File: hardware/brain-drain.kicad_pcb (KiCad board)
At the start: 4 copper layers, 180 x 110 mm, 311 parts, among them J10 SATA 22-pin, J11 SATA 22-pin, J12 SATA 22-pin, J13 SATA 22-pin, J21 KPJX-4S-S, J3 microSD, J4 RJ45 GbE magjack UDE RB1-125B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, J40 Fan GND/5V/TACH/PWM, J41 OLED GND/VCC/SCL/SDA, J5 USB-C rpiboot, J50 M.2 M-key, J6 nRPIBOOT, J7 UART0 GND/TX/RX, M1 CM5002016, Q1 2N7002, Q20 AO4407A, Q31 P-FET -30V 6A DFN3x3, Q32 P-FET -30V 6A DFN3x3, Q33 P-FET -30V 6A DFN3x3, Q34 P-FET -30V 6A DFN3x3, Q41 P-FET -30V 6A DFN3x3, Q42 P-FET -30V 6A DFN3x3, Q43 P-FET -30V 6A DFN3x3, Q44 P-FET -30V 6A DFN3x3, Q51 2N7002, Q52 2N7002, Q53 2N7002, Q54 2N7002, Q61 2N7002, Q62 2N7002, Q63 2N7002, Q64 2N7002, SW1 DIP x8, SW3 door microswitch, U1 USB5744/2G, U10 ASM1153E, U11 ASM1153E, U12 ASM1153E, U13 ASM1153E, U2 USB5744/2G, U20 TPS56637RPAR, U21 TPS56637RPAR, U22 AP63203WU-7, U3 AP2112K-1.2, U50 TPS22965DSGR, U51 AP63203WU-7, U52 TPS22965DSGR, Y1 25MHz CL=20pF, Y10 30MHz CL=16pF, Y11 30MHz CL=16pF, Y12 30MHz CL=16pF, Y13 30MHz CL=16pF, Y2 25MHz CL=20pF

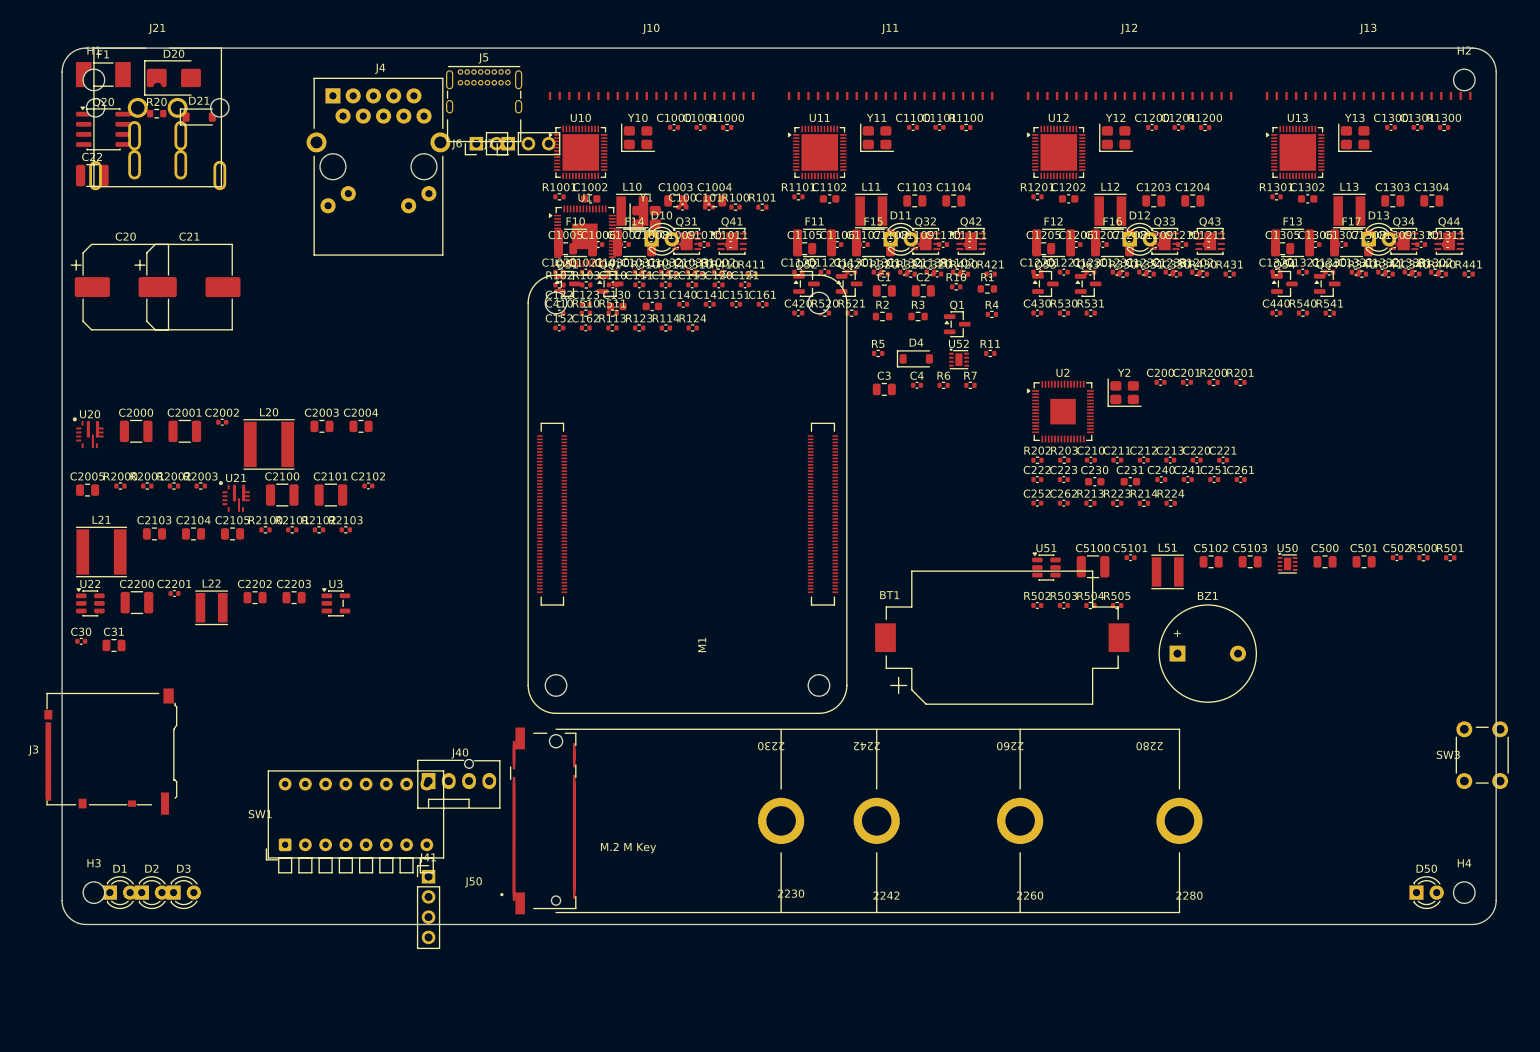
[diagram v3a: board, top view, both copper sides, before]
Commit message: docs: README with logo and renders, docs index, STATUS, USAGE, HISTORY, testing tracker, AGENT.md, changelog; enclosure refinements and renders; routing pipeline
Co-Authored-By: Claude Fable 5.1 <noreply@anthropic.com>
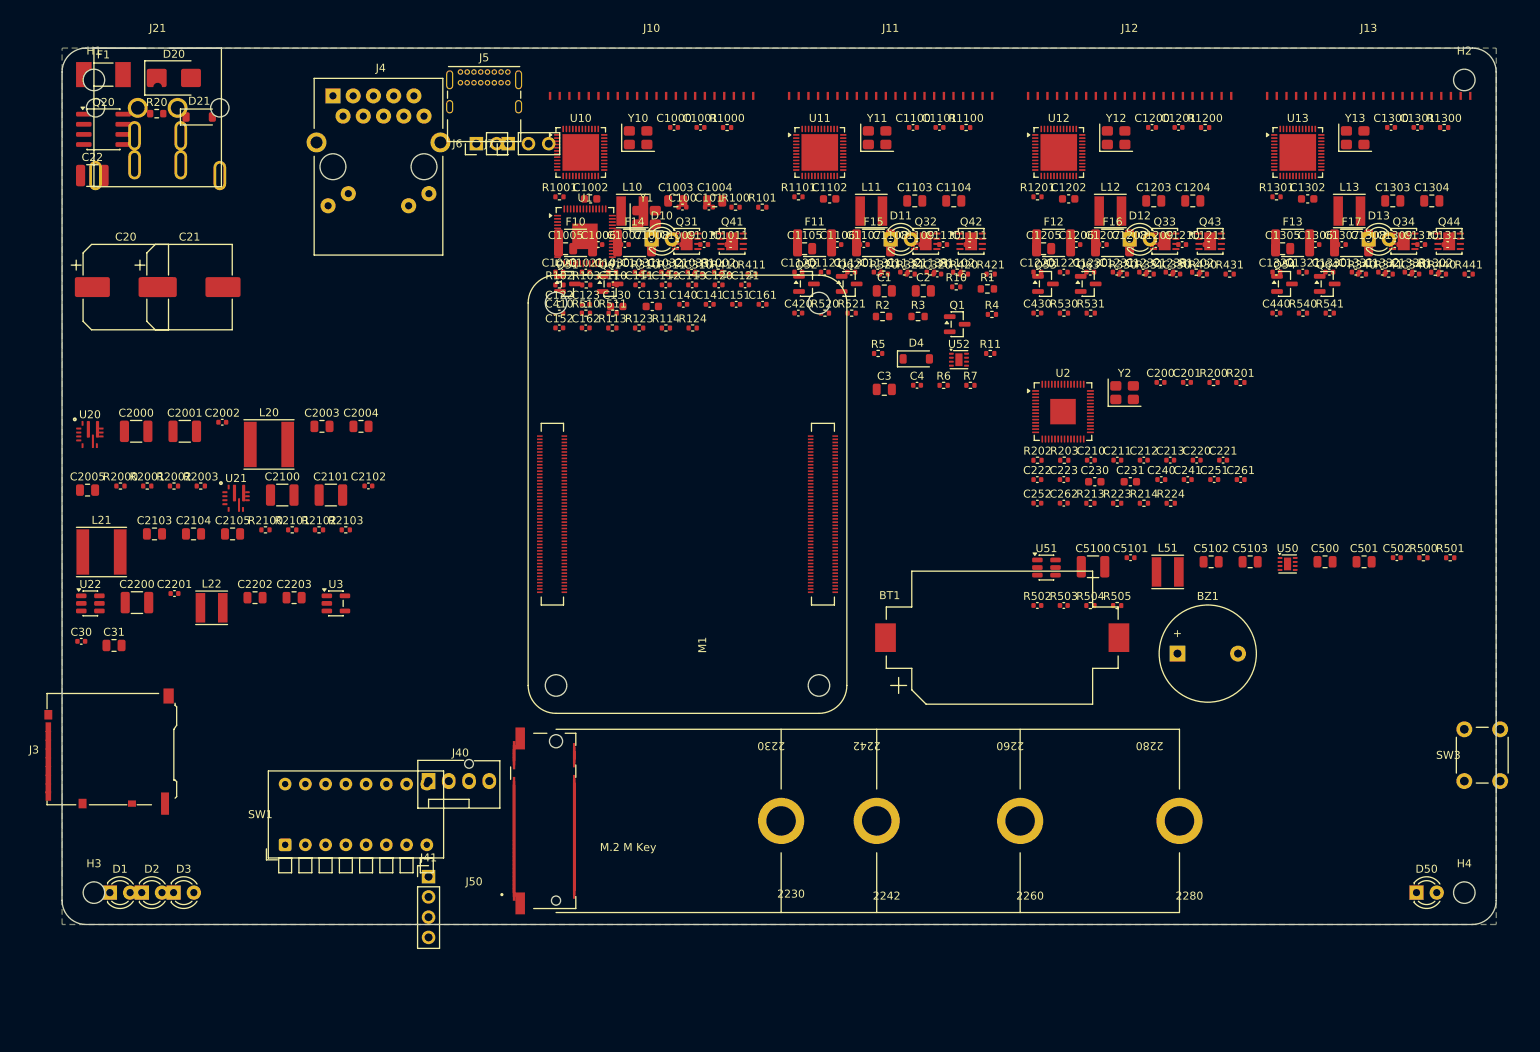
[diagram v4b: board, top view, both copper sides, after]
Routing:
- added copper zone on In2.Cu, net +12V
- added copper zone on In2.Cu, net +3V3
- added copper zone on In2.Cu, net 5V_HDD
- added copper zone on In2.Cu, net 5V_SYS
- added copper zone on B.Cu, net GND
- added copper zone on In1.Cu, net GND

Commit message: hw(board): DRC-clean placement (pad rotation fix, packer with capacity checks, USB-C on the left wall, DIN pad fix)
Co-Authored-By: Claude Fable 5.1 <noreply@anthropic.com>
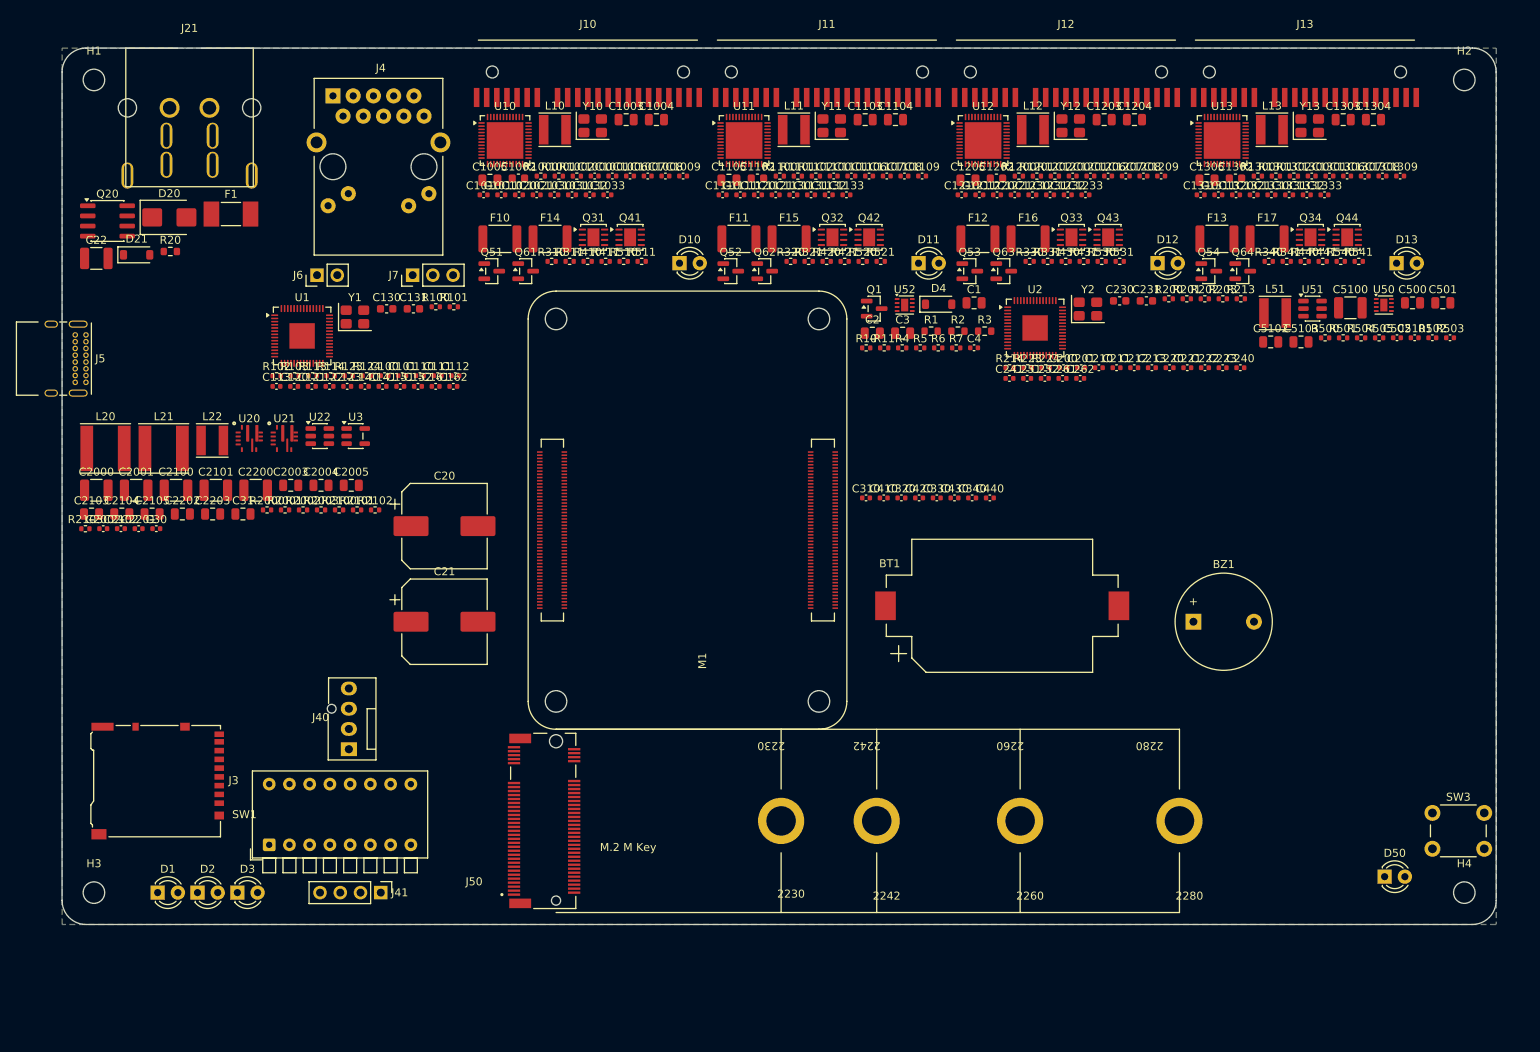
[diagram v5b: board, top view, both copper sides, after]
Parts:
- BT1: renamed from R20; value 100k -> CR2032; footprint Resistor_SMD:R_0603_1608Metric -> Battery:BatteryHolder_Keystone_1060_1x2032
- BZ1: renamed from C2002; value 100n 25V -> 5V magnetic; footprint Capacitor_SMD:C_0402_1005Metric -> Buzzer_Beeper:Buzzer_12x9.5RM7.6
- C1: renamed from C110; value 100n -> 22u 10V; footprint Capacitor_SMD:C_0402_1005Metric -> Capacitor_SMD:C_0805_2012Metric
- C100: renamed from R201; value 10k -> 33p; footprint Resistor_SMD:R_0402_1005Metric -> Capacitor_SMD:C_0402_1005Metric
- C1002: renamed from F14; value 2A hold 1812 -> 2.2u; footprint Fuse:Fuse_1812_4532Metric -> Capacitor_SMD:C_0603_1608Metric
- C1003: renamed from D10; value blue bay activity -> 10u 10V; footprint LED_THT:LED_D3.0mm -> Capacitor_SMD:C_0805_2012Metric
- C1004: renamed from R1002; value 470 -> 10u 10V; footprint Resistor_SMD:R_0402_1005Metric -> Capacitor_SMD:C_0805_2012Metric
- C1005: renamed from F10; value 3A hold 1812 -> 10u 10V; footprint Fuse:Fuse_1812_4532Metric -> Capacitor_SMD:C_0805_2012Metric
- C1006: renamed from R1100; value 12.1k 1% -> 100n; footprint Resistor_SMD:R_0402_1005Metric -> Capacitor_SMD:C_0402_1005Metric
- C1007: renamed from R1101; value 10k -> 100n; footprint Resistor_SMD:R_0402_1005Metric -> Capacitor_SMD:C_0402_1005Metric
- C1008: renamed from C1102; value 2.2u -> 100n; footprint Capacitor_SMD:C_0603_1608Metric -> Capacitor_SMD:C_0402_1005Metric
- C1009: renamed from L11; value 4.7u 1A -> 100n; footprint Inductor_SMD:L_Taiyo-Yuden_NR-40xx -> Capacitor_SMD:C_0402_1005Metric
- C101: renamed from R202; value 10k -> 33p; footprint Resistor_SMD:R_0402_1005Metric -> Capacitor_SMD:C_0402_1005Metric
- C1010: renamed from C1103; value 10u 10V -> 100n; footprint Capacitor_SMD:C_0805_2012Metric -> Capacitor_SMD:C_0402_1005Metric
- C1011: renamed from C1104; value 10u 10V -> 100n; footprint Capacitor_SMD:C_0805_2012Metric -> Capacitor_SMD:C_0402_1005Metric
- C1020: renamed from C1105; value 10u 10V -> 100n; footprint Capacitor_SMD:C_0805_2012Metric -> Capacitor_SMD:C_0402_1005Metric
- C1030: renamed from C1107; value 100n -> 10n
- C1031: renamed from C1108; value 100n -> 10n
- C1032: renamed from C1109; value 100n -> 10n
- C1033: renamed from C1110; value 100n -> 10n
- C110: renamed from R203; value 200k -> 100n; footprint Resistor_SMD:R_0402_1005Metric -> Capacitor_SMD:C_0402_1005Metric
- C1100: renamed from C1207; value 100n -> 22p
- C1101: renamed from C1208; value 100n -> 22p
- C1102: renamed from C1203; value 10u 10V -> 2.2u; footprint Capacitor_SMD:C_0805_2012Metric -> Capacitor_SMD:C_0603_1608Metric
- C1103: renamed from R1201; value 10k -> 10u 10V; footprint Resistor_SMD:R_0402_1005Metric -> Capacitor_SMD:C_0805_2012Metric
- C1104: renamed from C1202; value 2.2u -> 10u 10V; footprint Capacitor_SMD:C_0603_1608Metric -> Capacitor_SMD:C_0805_2012Metric
- C1105: renamed from L12; value 4.7u 1A -> 10u 10V; footprint Inductor_SMD:L_Taiyo-Yuden_NR-40xx -> Capacitor_SMD:C_0805_2012Metric
- C1111: renamed from C1230; value 10n -> 100n
- C1120: renamed from C1231; value 10n -> 100n
- C1121: renamed from C1232; value 10n -> 100n
- C1131: renamed from D12; value blue bay activity -> 10n; footprint LED_THT:LED_D3.0mm -> Capacitor_SMD:C_0402_1005Metric
- C1132: renamed from R1202; value 470 -> 10n; footprint Resistor_SMD:R_0402_1005Metric -> Capacitor_SMD:C_0402_1005Metric
- C1133: renamed from F12; value 3A hold 1812 -> 10n; footprint Fuse:Fuse_1812_4532Metric -> Capacitor_SMD:C_0402_1005Metric
- C1200: renamed from C1333; value 10n -> 22p
- C1201: renamed from D13; value blue bay activity -> 22p; footprint LED_THT:LED_D3.0mm -> Capacitor_SMD:C_0402_1005Metric
- C1202: renamed from C1321; value 100n -> 2.2u; footprint Capacitor_SMD:C_0402_1005Metric -> Capacitor_SMD:C_0603_1608Metric
- C1203: renamed from C1310; value 100n -> 10u 10V; footprint Capacitor_SMD:C_0402_1005Metric -> Capacitor_SMD:C_0805_2012Metric
- C1204: renamed from C1311; value 100n -> 10u 10V; footprint Capacitor_SMD:C_0402_1005Metric -> Capacitor_SMD:C_0805_2012Metric
- C1205: renamed from C1320; value 100n -> 10u 10V; footprint Capacitor_SMD:C_0402_1005Metric -> Capacitor_SMD:C_0805_2012Metric
- C1206: renamed from R1302; value 470 -> 100n; footprint Resistor_SMD:R_0402_1005Metric -> Capacitor_SMD:C_0402_1005Metric
- C1207: renamed from F13; value 3A hold 1812 -> 100n; footprint Fuse:Fuse_1812_4532Metric -> Capacitor_SMD:C_0402_1005Metric
- C1208: renamed from F17; value 2A hold 1812 -> 100n; footprint Fuse:Fuse_1812_4532Metric -> Capacitor_SMD:C_0402_1005Metric
- C1209: renamed from Q31; value P-FET -30V 6A DFN3x3 -> 100n; footprint Package_DFN_QFN:DFN-8-1EP_3x3mm_P0.65mm_EP1.5x2.25mm -> Capacitor_SMD:C_0402_1005Metric
- C1210: renamed from Q41; value P-FET -30V 6A DFN3x3 -> 100n; footprint Package_DFN_QFN:DFN-8-1EP_3x3mm_P0.65mm_EP1.5x2.25mm -> Capacitor_SMD:C_0402_1005Metric
- C1211: renamed from Q51; value 2N7002 -> 100n; footprint Package_TO_SOT_SMD:SOT-23 -> Capacitor_SMD:C_0402_1005Metric
- C1220: renamed from Q61; value 2N7002 -> 100n; footprint Package_TO_SOT_SMD:SOT-23 -> Capacitor_SMD:C_0402_1005Metric
- C1221: renamed from R310; value 100k -> 100n; footprint Resistor_SMD:R_0402_1005Metric -> Capacitor_SMD:C_0402_1005Metric
- C1230: renamed from R311; value 10k -> 10n; footprint Resistor_SMD:R_0402_1005Metric -> Capacitor_SMD:C_0402_1005Metric
- C1231: renamed from C310; value 100n -> 10n
- C1232: renamed from R410; value 100k -> 10n; footprint Resistor_SMD:R_0402_1005Metric -> Capacitor_SMD:C_0402_1005Metric
- C1233: renamed from R411; value 10k -> 10n; footprint Resistor_SMD:R_0402_1005Metric -> Capacitor_SMD:C_0402_1005Metric
- C130: renamed from C162; value 100n -> 4.7u 10V; footprint Capacitor_SMD:C_0402_1005Metric -> Capacitor_SMD:C_0603_1608Metric
- C1300: renamed from C430; value 100n -> 22p
- C1301: renamed from R530; value 10k -> 22p; footprint Resistor_SMD:R_0402_1005Metric -> Capacitor_SMD:C_0402_1005Metric
- C1302: renamed from R331; value 10k -> 2.2u; footprint Resistor_SMD:R_0402_1005Metric -> Capacitor_SMD:C_0603_1608Metric
- C1303: renamed from Q53; value 2N7002 -> 10u 10V; footprint Package_TO_SOT_SMD:SOT-23 -> Capacitor_SMD:C_0805_2012Metric
- C1304: renamed from Q63; value 2N7002 -> 10u 10V; footprint Package_TO_SOT_SMD:SOT-23 -> Capacitor_SMD:C_0805_2012Metric
- C1305: renamed from R330; value 100k -> 10u 10V; footprint Resistor_SMD:R_0402_1005Metric -> Capacitor_SMD:C_0805_2012Metric
- C1306: renamed from R531; value 1k -> 100n; footprint Resistor_SMD:R_0402_1005Metric -> Capacitor_SMD:C_0402_1005Metric
- C1307: renamed from Q34; value P-FET -30V 6A DFN3x3 -> 100n; footprint Package_DFN_QFN:DFN-8-1EP_3x3mm_P0.65mm_EP1.5x2.25mm -> Capacitor_SMD:C_0402_1005Metric
- C1308: renamed from Q44; value P-FET -30V 6A DFN3x3 -> 100n; footprint Package_DFN_QFN:DFN-8-1EP_3x3mm_P0.65mm_EP1.5x2.25mm -> Capacitor_SMD:C_0402_1005Metric
- C1309: renamed from Q54; value 2N7002 -> 100n; footprint Package_TO_SOT_SMD:SOT-23 -> Capacitor_SMD:C_0402_1005Metric
- C131: renamed from R113; value 10k -> 4.7u 10V; footprint Resistor_SMD:R_0402_1005Metric -> Capacitor_SMD:C_0603_1608Metric
- C1310: renamed from Q64; value 2N7002 -> 100n; footprint Package_TO_SOT_SMD:SOT-23 -> Capacitor_SMD:C_0402_1005Metric
- C1311: renamed from R340; value 100k -> 100n; footprint Resistor_SMD:R_0402_1005Metric -> Capacitor_SMD:C_0402_1005Metric
- C1320: renamed from R341; value 10k -> 100n; footprint Resistor_SMD:R_0402_1005Metric -> Capacitor_SMD:C_0402_1005Metric
- C1330: renamed from R440; value 100k -> 10n; footprint Resistor_SMD:R_0402_1005Metric -> Capacitor_SMD:C_0402_1005Metric
- C1331: renamed from R441; value 10k -> 10n; footprint Resistor_SMD:R_0402_1005Metric -> Capacitor_SMD:C_0402_1005Metric
- C1332: renamed from C440; value 100n -> 10n
- C1333: renamed from R540; value 10k -> 10n; footprint Resistor_SMD:R_0402_1005Metric -> Capacitor_SMD:C_0402_1005Metric
- C141: renamed from C230; value 4.7u 10V -> 100n; footprint Capacitor_SMD:C_0603_1608Metric -> Capacitor_SMD:C_0402_1005Metric
- C151: renamed from C231; value 4.7u 10V -> 100n; footprint Capacitor_SMD:C_0603_1608Metric -> Capacitor_SMD:C_0402_1005Metric
- C2: renamed from C111; value 100n -> 22u 10V; footprint Capacitor_SMD:C_0402_1005Metric -> Capacitor_SMD:C_0805_2012Metric
- C20: renamed from F1; value 10A slow 0453010.MR -> 680u 25V low-ESR; footprint Fuse:Fuse_Littelfuse-NANO2-451_453 -> Capacitor_SMD:CP_Elec_10x10.5
- C200: renamed from R1000; value 12.1k 1% -> 33p; footprint Resistor_SMD:R_0402_1005Metric -> Capacitor_SMD:C_0402_1005Metric
- C2000: renamed from C5101; value 100n 10V -> 10u 25V; footprint Capacitor_SMD:C_0402_1005Metric -> Capacitor_SMD:C_1210_3225Metric
- C2001: renamed from L51; value 4.7u 3A -> 10u 25V; footprint Inductor_SMD:L_Taiyo-Yuden_NR-40xx -> Capacitor_SMD:C_1210_3225Metric
- C2002: renamed from BZ1; value 5V magnetic -> 100n 25V; footprint Buzzer_Beeper:Buzzer_12x9.5RM7.6 -> Capacitor_SMD:C_0402_1005Metric
- C2003: renamed from C30; value 1u 10V -> 22u 10V; footprint Capacitor_SMD:C_0402_1005Metric -> Capacitor_SMD:C_0805_2012Metric
- C2004: renamed from C31; value 10u 10V -> 22u 10V
- C2005: renamed from M1; value CM5002016 -> 22u 10V; footprint brain-drain:Raspberry-Pi-5-Compute-Module -> Capacitor_SMD:C_0805_2012Metric
- C201: renamed from R1001; value 10k -> 33p; footprint Resistor_SMD:R_0402_1005Metric -> Capacitor_SMD:C_0402_1005Metric
- C21: renamed from D20; value SMBJ15A -> 680u 25V low-ESR; footprint Diode_SMD:D_SMB -> Capacitor_SMD:CP_Elec_10x10.5
- C210: renamed from C1002; value 2.2u -> 100n; footprint Capacitor_SMD:C_0603_1608Metric -> Capacitor_SMD:C_0402_1005Metric
- C2100: renamed from C5102; value 22u 10V -> 10u 25V; footprint Capacitor_SMD:C_0805_2012Metric -> Capacitor_SMD:C_1210_3225Metric
- C2101: renamed from C5103; value 22u 10V -> 10u 25V; footprint Capacitor_SMD:C_0805_2012Metric -> Capacitor_SMD:C_1210_3225Metric
- C2102: renamed from Q1; value 2N7002 -> 100n 25V; footprint Package_TO_SOT_SMD:SOT-23 -> Capacitor_SMD:C_0402_1005Metric
- C2105: renamed from BT1; value CR2032 -> 22u 10V; footprint Battery:BatteryHolder_Keystone_1060_1x2032 -> Capacitor_SMD:C_0805_2012Metric
- C211: renamed from L10; value 4.7u 1A -> 100n; footprint Inductor_SMD:L_Taiyo-Yuden_NR-40xx -> Capacitor_SMD:C_0402_1005Metric
- C212: renamed from C1003; value 10u 10V -> 100n; footprint Capacitor_SMD:C_0805_2012Metric -> Capacitor_SMD:C_0402_1005Metric
- C213: renamed from C1004; value 10u 10V -> 100n; footprint Capacitor_SMD:C_0805_2012Metric -> Capacitor_SMD:C_0402_1005Metric
- C22: renamed from R2102; value 100k -> 10u 25V; footprint Resistor_SMD:R_0402_1005Metric -> Capacitor_SMD:C_1210_3225Metric
- C220: renamed from C1005; value 10u 10V -> 100n; footprint Capacitor_SMD:C_0805_2012Metric -> Capacitor_SMD:C_0402_1005Metric
- C2200: renamed from U3; value AP2112K-1.2 -> 10u 25V; footprint Package_TO_SOT_SMD:SOT-23-5 -> Capacitor_SMD:C_1210_3225Metric
- C2201: renamed from R4; value 1k -> 100n 10V; footprint Resistor_SMD:R_0402_1005Metric -> Capacitor_SMD:C_0402_1005Metric
- C2202: renamed from J6; value nRPIBOOT -> 22u 10V; footprint Connector_PinHeader_2.54mm:PinHeader_1x02_P2.54mm_Vertical -> Capacitor_SMD:C_0805_2012Metric
- C2203: renamed from J7; value UART0 GND/TX/RX -> 22u 10V; footprint Connector_PinHeader_2.54mm:PinHeader_1x03_P2.54mm_Vertical -> Capacitor_SMD:C_0805_2012Metric
- C230: renamed from C262; value 100n -> 4.7u 10V; footprint Capacitor_SMD:C_0402_1005Metric -> Capacitor_SMD:C_0603_1608Metric
- C231: renamed from R213; value 10k -> 4.7u 10V; footprint Resistor_SMD:R_0402_1005Metric -> Capacitor_SMD:C_0603_1608Metric
- C262: renamed from C1030; value 10n -> 100n
- C3: renamed from C112; value 100n -> 10u 10V; footprint Capacitor_SMD:C_0402_1005Metric -> Capacitor_SMD:C_0805_2012Metric
- C30: renamed from R5; value 100k -> 1u 10V; footprint Resistor_SMD:R_0402_1005Metric -> Capacitor_SMD:C_0402_1005Metric
- C31: renamed from J40; value Fan GND/5V/TACH/PWM -> 10u 10V; footprint Connector:FanPinHeader_1x04_P2.54mm_Vertical -> Capacitor_SMD:C_0805_2012Metric
- C310: renamed from J12; value SATA 22-pin -> 100n; footprint brain-drain:SATA_22pin_Receptacle_RA -> Capacitor_SMD:C_0402_1005Metric
- C320: renamed from C1305; value 10u 10V -> 100n; footprint Capacitor_SMD:C_0805_2012Metric -> Capacitor_SMD:C_0402_1005Metric
- C340: renamed from D50; value blue M.2 activity -> 100n; footprint LED_THT:LED_D3.0mm -> Capacitor_SMD:C_0402_1005Metric
- C4: renamed from C151; value 100n -> 1u 10V
- C410: renamed from Y12; value 30MHz CL=16pF -> 100n; footprint Crystal:Crystal_SMD_3225-4Pin_3.2x2.5mm -> Capacitor_SMD:C_0402_1005Metric
- C430: renamed from R520; value 10k -> 100n; footprint Resistor_SMD:R_0402_1005Metric -> Capacitor_SMD:C_0402_1005Metric
- C440: renamed from SW3; value door microswitch -> 100n; footprint Button_Switch_THT:SW_PUSH_6mm -> Capacitor_SMD:C_0402_1005Metric
- C500: renamed from R11; value 10k -> 10u 10V; footprint Resistor_SMD:R_0402_1005Metric -> Capacitor_SMD:C_0805_2012Metric
- C501: renamed from C3; value 10u 10V -> 22u 10V
- C502: renamed from Y1; value 25MHz CL=20pF -> 1n; footprint Crystal:Crystal_SMD_3225-4Pin_3.2x2.5mm -> Capacitor_SMD:C_0402_1005Metric
- C5100: renamed from J3; value microSD -> 10u 25V; footprint Connector_Card:microSD_HC_Hirose_DM3AT-SF-PEJM5 -> Capacitor_SMD:C_1210_3225Metric
- C5101: renamed from C100; value 33p -> 100n 10V
- C5102: renamed from C4; value 1u 10V -> 22u 10V; footprint Capacitor_SMD:C_0402_1005Metric -> Capacitor_SMD:C_0805_2012Metric
- C5103: renamed from J4; value RJ45 GbE magjack UDE RB1-125B8G1A -> 22u 10V; footprint Connector_RJ:RJ45_UDE_RB1-125B8G1A -> Capacitor_SMD:C_0805_2012Metric
- D1: renamed from C22; value 10u 25V -> green PWR; footprint Capacitor_SMD:C_1210_3225Metric -> LED_THT:LED_D3.0mm
- D10: renamed from R2001; value 10k -> blue bay activity; footprint Resistor_SMD:R_0402_1005Metric -> LED_THT:LED_D3.0mm
- D11: renamed from R2003; value 10k -> blue bay activity; footprint Resistor_SMD:R_0402_1005Metric -> LED_THT:LED_D3.0mm
- D12: renamed from C2100; value 10u 25V -> blue bay activity; footprint Capacitor_SMD:C_1210_3225Metric -> LED_THT:LED_D3.0mm
- D13: renamed from C2102; value 100n 25V -> blue bay activity; footprint Capacitor_SMD:C_0402_1005Metric -> LED_THT:LED_D3.0mm
- D2: renamed from U20; value TPS56637RPAR -> green ACT; footprint brain-drain:Texas_RPA0010A_VQFN-HR-10_3x3mm -> LED_THT:LED_D3.0mm
- D20: renamed from R2100; value 73.2k -> SMBJ15A; footprint Resistor_SMD:R_0402_1005Metric -> Diode_SMD:D_SMB
- D21: renamed from R2103; value 10k -> 12V 0.5W; footprint Resistor_SMD:R_0402_1005Metric -> Diode_SMD:D_SOD-123
- D3: renamed from C2000; value 10u 25V -> red STATUS; footprint Capacitor_SMD:C_1210_3225Metric -> LED_THT:LED_D3.0mm
- D4: renamed from R103; value 200k -> 1N4148W; footprint Resistor_SMD:R_0402_1005Metric -> Diode_SMD:D_SOD-123
- D50: renamed from C2103; value 22u 10V -> blue M.2 activity; footprint Capacitor_SMD:C_0805_2012Metric -> LED_THT:LED_D3.0mm
- F1: renamed from R2101; value 10k -> 10A slow 0453010.MR; footprint Resistor_SMD:R_0402_1005Metric -> Fuse:Fuse_Littelfuse-NANO2-451_453
- F10: renamed from C1111; value 100n -> 3A hold 1812; footprint Capacitor_SMD:C_0402_1005Metric -> Fuse:Fuse_1812_4532Metric
- F11: renamed from F16; value 2A hold 1812 -> 3A hold 1812
- F12: renamed from C410; value 100n -> 3A hold 1812; footprint Capacitor_SMD:C_0402_1005Metric -> Fuse:Fuse_1812_4532Metric
- F13: renamed from R541; value 1k -> 3A hold 1812; footprint Resistor_SMD:R_0402_1005Metric -> Fuse:Fuse_1812_4532Metric
- F14: renamed from C1120; value 100n -> 2A hold 1812; footprint Capacitor_SMD:C_0402_1005Metric -> Fuse:Fuse_1812_4532Metric
- F15: renamed from U13; value ASM1153E -> 2A hold 1812; footprint Package_DFN_QFN:QFN-48-1EP_6x6mm_P0.4mm_EP4.6x4.6mm -> Fuse:Fuse_1812_4532Metric
- F16: renamed from R510; value 10k -> 2A hold 1812; footprint Resistor_SMD:R_0402_1005Metric -> Fuse:Fuse_1812_4532Metric
- F17: renamed from J50; value M.2 M-key -> 2A hold 1812; footprint brain-drain:M2_Socket3_MKey_CM5IO -> Fuse:Fuse_1812_4532Metric
- J10: renamed from R2000; value 73.2k -> SATA 22-pin; footprint Resistor_SMD:R_0402_1005Metric -> brain-drain:SATA_22pin_Receptacle_RA
- J11: renamed from R2002; value 100k -> SATA 22-pin; footprint Resistor_SMD:R_0402_1005Metric -> brain-drain:SATA_22pin_Receptacle_RA
- J12: renamed from U21; value TPS56637RPAR -> SATA 22-pin; footprint brain-drain:Texas_RPA0010A_VQFN-HR-10_3x3mm -> brain-drain:SATA_22pin_Receptacle_RA
- J13: renamed from C2101; value 10u 25V -> SATA 22-pin; footprint Capacitor_SMD:C_1210_3225Metric -> brain-drain:SATA_22pin_Receptacle_RA
- J3: renamed from C2003; value 22u 10V -> microSD; footprint Capacitor_SMD:C_0805_2012Metric -> Connector_Card:microSD_HC_Hirose_DM3AT-SF-PEJM5
- J4: renamed from C2004; value 22u 10V -> RJ45 GbE magjack UDE RB1-125B8G1A; footprint Capacitor_SMD:C_0805_2012Metric -> Connector_RJ:RJ45_UDE_RB1-125B8G1A
- J40: renamed from C21; value 680u 25V low-ESR -> Fan GND/5V/TACH/PWM; footprint Capacitor_SMD:CP_Elec_10x10.5 -> Connector:FanPinHeader_1x04_P2.54mm_Vertical
- J41: renamed from L20; value 2.2u 8A -> OLED GND/VCC/SCL/SDA; footprint Inductor_SMD:L_Taiyo-Yuden_NR-60xx -> Connector_PinHeader_2.54mm:PinHeader_1x04_P2.54mm_Vertical
- J5: renamed from C2005; value 22u 10V -> USB-C rpiboot; footprint Capacitor_SMD:C_0805_2012Metric -> Connector_USB:USB_C_Receptacle_GCT_USB4085
- J50: renamed from L21; value 2.2u 8A -> M.2 M-key; footprint Inductor_SMD:L_Taiyo-Yuden_NR-60xx -> brain-drain:M2_Socket3_MKey_CM5IO
- J6: renamed from D21; value 12V 0.5W -> nRPIBOOT; footprint Diode_SMD:D_SOD-123 -> Connector_PinHeader_2.54mm:PinHeader_1x02_P2.54mm_Vertical
- J7: renamed from C20; value 680u 25V low-ESR -> UART0 GND/TX/RX; footprint Capacitor_SMD:CP_Elec_10x10.5 -> Connector_PinHeader_2.54mm:PinHeader_1x03_P2.54mm_Vertical
- L10: renamed from C1032; value 10n -> 4.7u 1A; footprint Capacitor_SMD:C_0402_1005Metric -> Inductor_SMD:L_Taiyo-Yuden_NR-40xx
- L11: renamed from C1201; value 22p -> 4.7u 1A; footprint Capacitor_SMD:C_0402_1005Metric -> Inductor_SMD:L_Taiyo-Yuden_NR-40xx
- L12: renamed from C1308; value 100n -> 4.7u 1A; footprint Capacitor_SMD:C_0402_1005Metric -> Inductor_SMD:L_Taiyo-Yuden_NR-40xx
- L13: renamed from Q33; value P-FET -30V 6A DFN3x3 -> 4.7u 1A; footprint Package_DFN_QFN:DFN-8-1EP_3x3mm_P0.65mm_EP1.5x2.25mm -> Inductor_SMD:L_Taiyo-Yuden_NR-40xx
- L20: renamed from C2200; value 10u 25V -> 2.2u 8A; footprint Capacitor_SMD:C_1210_3225Metric -> Inductor_SMD:L_Taiyo-Yuden_NR-60xx
- L21: renamed from C2201; value 100n 10V -> 2.2u 8A; footprint Capacitor_SMD:C_0402_1005Metric -> Inductor_SMD:L_Taiyo-Yuden_NR-60xx
- L51: renamed from D4; value 1N4148W -> 4.7u 3A; footprint Diode_SMD:D_SOD-123 -> Inductor_SMD:L_Taiyo-Yuden_NR-40xx
- M1: renamed from Q20; value AO4407A -> CM5002016; footprint Package_SO:SOIC-8_3.9x4.9mm_P1.27mm -> brain-drain:Raspberry-Pi-5-Compute-Module
- Q1: renamed from R101; value 10k -> 2N7002; footprint Resistor_SMD:R_0402_1005Metric -> Package_TO_SOT_SMD:SOT-23
- Q20: renamed from C2105; value 22u 10V -> AO4407A; footprint Capacitor_SMD:C_0805_2012Metric -> Package_SO:SOIC-8_3.9x4.9mm_P1.27mm
- Q31: renamed from C1121; value 100n -> P-FET -30V 6A DFN3x3; footprint Capacitor_SMD:C_0402_1005Metric -> Package_DFN_QFN:DFN-8-1EP_3x3mm_P0.65mm_EP1.5x2.25mm
- Q32: renamed from J13; value SATA 22-pin -> P-FET -30V 6A DFN3x3; footprint brain-drain:SATA_22pin_Receptacle_RA -> Package_DFN_QFN:DFN-8-1EP_3x3mm_P0.65mm_EP1.5x2.25mm
- Q33: renamed from R511; value 1k -> P-FET -30V 6A DFN3x3; footprint Resistor_SMD:R_0402_1005Metric -> Package_DFN_QFN:DFN-8-1EP_3x3mm_P0.65mm_EP1.5x2.25mm
- Q34: renamed from U50; value TPS22965DSGR -> P-FET -30V 6A DFN3x3; footprint Package_SON:Texas_DSG0008A_WSON-8-1EP_2x2mm_P0.5mm_EP0.9x1.6mm -> Package_DFN_QFN:DFN-8-1EP_3x3mm_P0.65mm_EP1.5x2.25mm
- Q41: renamed from C1130; value 10n -> P-FET -30V 6A DFN3x3; footprint Capacitor_SMD:C_0402_1005Metric -> Package_DFN_QFN:DFN-8-1EP_3x3mm_P0.65mm_EP1.5x2.25mm
- Q42: renamed from Y13; value 30MHz CL=16pF -> P-FET -30V 6A DFN3x3; footprint Crystal:Crystal_SMD_3225-4Pin_3.2x2.5mm -> Package_DFN_QFN:DFN-8-1EP_3x3mm_P0.65mm_EP1.5x2.25mm
- Q44: renamed from C500; value 10u 10V -> P-FET -30V 6A DFN3x3; footprint Capacitor_SMD:C_0805_2012Metric -> Package_DFN_QFN:DFN-8-1EP_3x3mm_P0.65mm_EP1.5x2.25mm
- Q51: renamed from C1131; value 10n -> 2N7002; footprint Capacitor_SMD:C_0402_1005Metric -> Package_TO_SOT_SMD:SOT-23
- Q52: renamed from C1300; value 22p -> 2N7002; footprint Capacitor_SMD:C_0402_1005Metric -> Package_TO_SOT_SMD:SOT-23
- Q53: renamed from Q42; value P-FET -30V 6A DFN3x3 -> 2N7002; footprint Package_DFN_QFN:DFN-8-1EP_3x3mm_P0.65mm_EP1.5x2.25mm -> Package_TO_SOT_SMD:SOT-23
- Q54: renamed from C501; value 22u 10V -> 2N7002; footprint Capacitor_SMD:C_0805_2012Metric -> Package_TO_SOT_SMD:SOT-23
- Q61: renamed from C1132; value 10n -> 2N7002; footprint Capacitor_SMD:C_0402_1005Metric -> Package_TO_SOT_SMD:SOT-23
- Q62: renamed from C1301; value 22p -> 2N7002; footprint Capacitor_SMD:C_0402_1005Metric -> Package_TO_SOT_SMD:SOT-23
- Q64: renamed from C502; value 1n -> 2N7002; footprint Capacitor_SMD:C_0402_1005Metric -> Package_TO_SOT_SMD:SOT-23
- R1: renamed from C113; value 100n -> 1k; footprint Capacitor_SMD:C_0402_1005Metric -> Resistor_SMD:R_0603_1608Metric
- R10: renamed from C122; value 100n -> 10k; footprint Capacitor_SMD:C_0402_1005Metric -> Resistor_SMD:R_0402_1005Metric
- R100: renamed from R123; value 10k -> 12.0k 1%
- R1000: renamed from U11; value ASM1153E -> 12.1k 1%; footprint Package_DFN_QFN:QFN-48-1EP_6x6mm_P0.4mm_EP4.6x4.6mm -> Resistor_SMD:R_0402_1005Metric
- R1001: renamed from J11; value SATA 22-pin -> 10k; footprint brain-drain:SATA_22pin_Receptacle_RA -> Resistor_SMD:R_0402_1005Metric
- R1002: renamed from Y11; value 30MHz CL=16pF -> 470; footprint Crystal:Crystal_SMD_3225-4Pin_3.2x2.5mm -> Resistor_SMD:R_0402_1005Metric
- R103: renamed from U2; value USB5744/2G -> 200k; footprint Package_DFN_QFN:QFN-56-1EP_7x7mm_P0.4mm_EP3.2x3.2mm -> Resistor_SMD:R_0402_1005Metric
- R11: renamed from C123; value 100n -> 10k; footprint Capacitor_SMD:C_0402_1005Metric -> Resistor_SMD:R_0402_1005Metric
- R1100: renamed from C1204; value 10u 10V -> 12.1k 1%; footprint Capacitor_SMD:C_0805_2012Metric -> Resistor_SMD:R_0402_1005Metric
- R1101: renamed from C1205; value 10u 10V -> 10k; footprint Capacitor_SMD:C_0805_2012Metric -> Resistor_SMD:R_0402_1005Metric
- R1102: renamed from C1206; value 100n -> 470; footprint Capacitor_SMD:C_0402_1005Metric -> Resistor_SMD:R_0402_1005Metric
- R113: renamed from Y2; value 25MHz CL=20pF -> 10k; footprint Crystal:Crystal_SMD_3225-4Pin_3.2x2.5mm -> Resistor_SMD:R_0402_1005Metric
- R114: renamed from C200; value 33p -> 10k; footprint Capacitor_SMD:C_0402_1005Metric -> Resistor_SMD:R_0402_1005Metric
- R1200: renamed from C1330; value 10n -> 12.1k 1%; footprint Capacitor_SMD:C_0402_1005Metric -> Resistor_SMD:R_0402_1005Metric
- R1201: renamed from C1331; value 10n -> 10k; footprint Capacitor_SMD:C_0402_1005Metric -> Resistor_SMD:R_0402_1005Metric
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- renumbered C1100 to C1000, C1101 to C1001, C1106 to C1021, C1209 to C1106, C1210 to C1107, C1211 to C1108, C1220 to C1109, C210 to C111, C1221 to C1110, C211 to C112, C212 to C113, C1233 to C1130, C213 to C120, C220 to C121, C221 to C122, C222 to C123, C340 to C1321, C223 to C140, C240 to C152, C241 to C161, C251 to C162, C1 to C2103, C2 to C2104, C1006 to C221, C1007 to C222, C1008 to C223, C1009 to C240, C1010 to C241, C1011 to C251, C1020 to C252, C1021 to C261, C420 to C330, C1306 to C420, Q32 to Q43, Q52 to Q63, R114 to R101, R124 to R102, R214 to R201, R224 to R202, R1301 to R321, R501 to R341, R504 to R540, U51 to U22, U52 to U50
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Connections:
- BT1 pad 1: Q20_GATE -> VBAT
- BZ1 pad 1: U20_BOOT -> 5V_SYS
- BZ1 pad 2: U20_SW -> BZ1_N
- C1 pad 1: +3V3 -> 5V_SYS
- C100 pad 1: +3V3 -> U1_XTALI
- C100 pad 2: U2_VBUS_DET -> GND
- C1000 pad 1: U11_XI -> U10_XI
- C1001 pad 1: U11_XO -> U10_XO
- C1002 pad 1: 5V_BAY1_SW -> U10_RST
- C1002 pad 2: 5V_BAY1 -> GND
- C1003 pad 1: U10_LED -> U10_VDD_CORE
- C1003 pad 2: BAY1_LED_A -> GND
- C1004 pad 1: U10_VCCO -> 5V_SYS
- C1004 pad 2: BAY1_LED_A -> GND
- C1005 pad 1: 12V_BAY1_SW -> U10_VCCO
- C1005 pad 2: 12V_BAY1 -> GND
- C1006 pad 1: U11_REXT -> U10_VDD_CORE
- C1007 pad 1: U11_VCCO -> U10_VDD_CORE
- C1007 pad 2: U11_RST -> GND
- C1008 pad 1: U11_RST -> U10_VCCO
- C1009 pad 1: U11_LXI -> U10_VCCO
- C1009 pad 2: U11_VDD_CORE -> GND
- C101 pad 1: +3V3 -> U1_XTALO
- C101 pad 2: U2_RESET_N -> GND
- C1010 pad 1: U11_VDD_CORE -> U10_VCCO
- C1011 pad 1: 5V_SYS -> U10_VCCO
- C1020 pad 1: U11_VCCO -> U10_UTXP
- C1020 pad 2: GND -> BAY1_USB3_TX_P
- C1021 pad 1: U11_VDD_CORE -> U10_UTXN
- C1021 pad 2: GND -> BAY1_USB3_TX_N
- C1030 pad 1: U11_VDD_CORE -> U10_STXP
- C1030 pad 2: GND -> BAY1_SATA_A_P
- C1031 pad 1: U11_VCCO -> U10_STXN
- C1031 pad 2: GND -> BAY1_SATA_A_N
- C1032 pad 1: U11_VCCO -> BAY1_SATA_B_P
- C1032 pad 2: GND -> U10_SRXP
- C1033 pad 1: U11_VCCO -> BAY1_SATA_B_N
- C1033 pad 2: GND -> U10_SRXN
- C110 pad 1: U2_CFG_NON_REM -> +3V3
- C1100 pad 1: U12_VDD_CORE -> U11_XI
- C1101 pad 1: U12_VCCO -> U11_XO
- C1102 pad 1: U12_VDD_CORE -> U11_RST
- C1103 pad 1: U12_VCCO -> U11_VDD_CORE
- C1103 pad 2: U12_RST -> GND
- C1104 pad 1: U12_RST -> 5V_SYS
- C1105 pad 1: U12_LXI -> U11_VCCO
- C1105 pad 2: U12_VDD_CORE -> GND
- C1106 pad 1: U12_VCCO -> U11_VDD_CORE
- C1107 pad 1: U12_VCCO -> U11_VDD_CORE
- C1108 pad 1: U12_VCCO -> U11_VCCO
- C1109 pad 1: U12_UTXP -> U11_VCCO
- C1109 pad 2: BAY3_USB3_TX_P -> GND
- C1110 pad 1: U12_UTXN -> U11_VCCO
- C1110 pad 2: BAY3_USB3_TX_N -> GND
- C1111 pad 1: U12_STXP -> U11_VCCO
- C1111 pad 2: BAY3_SATA_A_P -> GND
- C1120 pad 1: U12_STXN -> U11_UTXP
- C1120 pad 2: BAY3_SATA_A_N -> BAY2_USB3_TX_P
- C1121 pad 1: BAY3_SATA_B_P -> U11_UTXN
- C1121 pad 2: U12_SRXP -> BAY2_USB3_TX_N
- C1130 pad 1: BAY3_SATA_B_N -> U11_STXP
- C1130 pad 2: U12_SRXN -> BAY2_SATA_A_P
- C1131 pad 1: U12_LED -> U11_STXN
- C1131 pad 2: BAY3_LED_A -> BAY2_SATA_A_N
- C1132 pad 1: U12_VCCO -> BAY2_SATA_B_P
- C1132 pad 2: BAY3_LED_A -> U11_SRXP
- C1133 pad 1: 12V_BAY3_SW -> BAY2_SATA_B_N
- C1133 pad 2: 12V_BAY3 -> U11_SRXN
- C120 pad 1: +3V3 -> +1V2
- C1200 pad 1: BAY4_SATA_B_N -> U12_XI
- C1200 pad 2: U13_SRXN -> GND
- C1201 pad 1: U13_LED -> U12_XO
- C1201 pad 2: BAY4_LED_A -> GND
- C1202 pad 1: U13_UTXN -> U12_RST
- C1202 pad 2: BAY4_USB3_TX_N -> GND
- C1203 pad 1: U13_VCCO -> U12_VDD_CORE
- C1204 pad 1: U13_VCCO -> 5V_SYS
- C1205 pad 1: U13_UTXP -> U12_VCCO
- C1205 pad 2: BAY4_USB3_TX_P -> GND
- C1206 pad 1: U13_VCCO -> U12_VDD_CORE
- C1206 pad 2: BAY4_LED_A -> GND
- C1207 pad 1: 12V_BAY4_SW -> U12_VDD_CORE
- C1207 pad 2: 12V_BAY4 -> GND
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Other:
- rule pad_to_mask_clearance: 0 -> 0.05

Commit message: hw(routing): autorouted signal nets imported (freerouting), CM5 hole keep-outs, hand-routing list; renders and status updated
Co-Authored-By: Claude Fable 5.1 <noreply@anthropic.com>
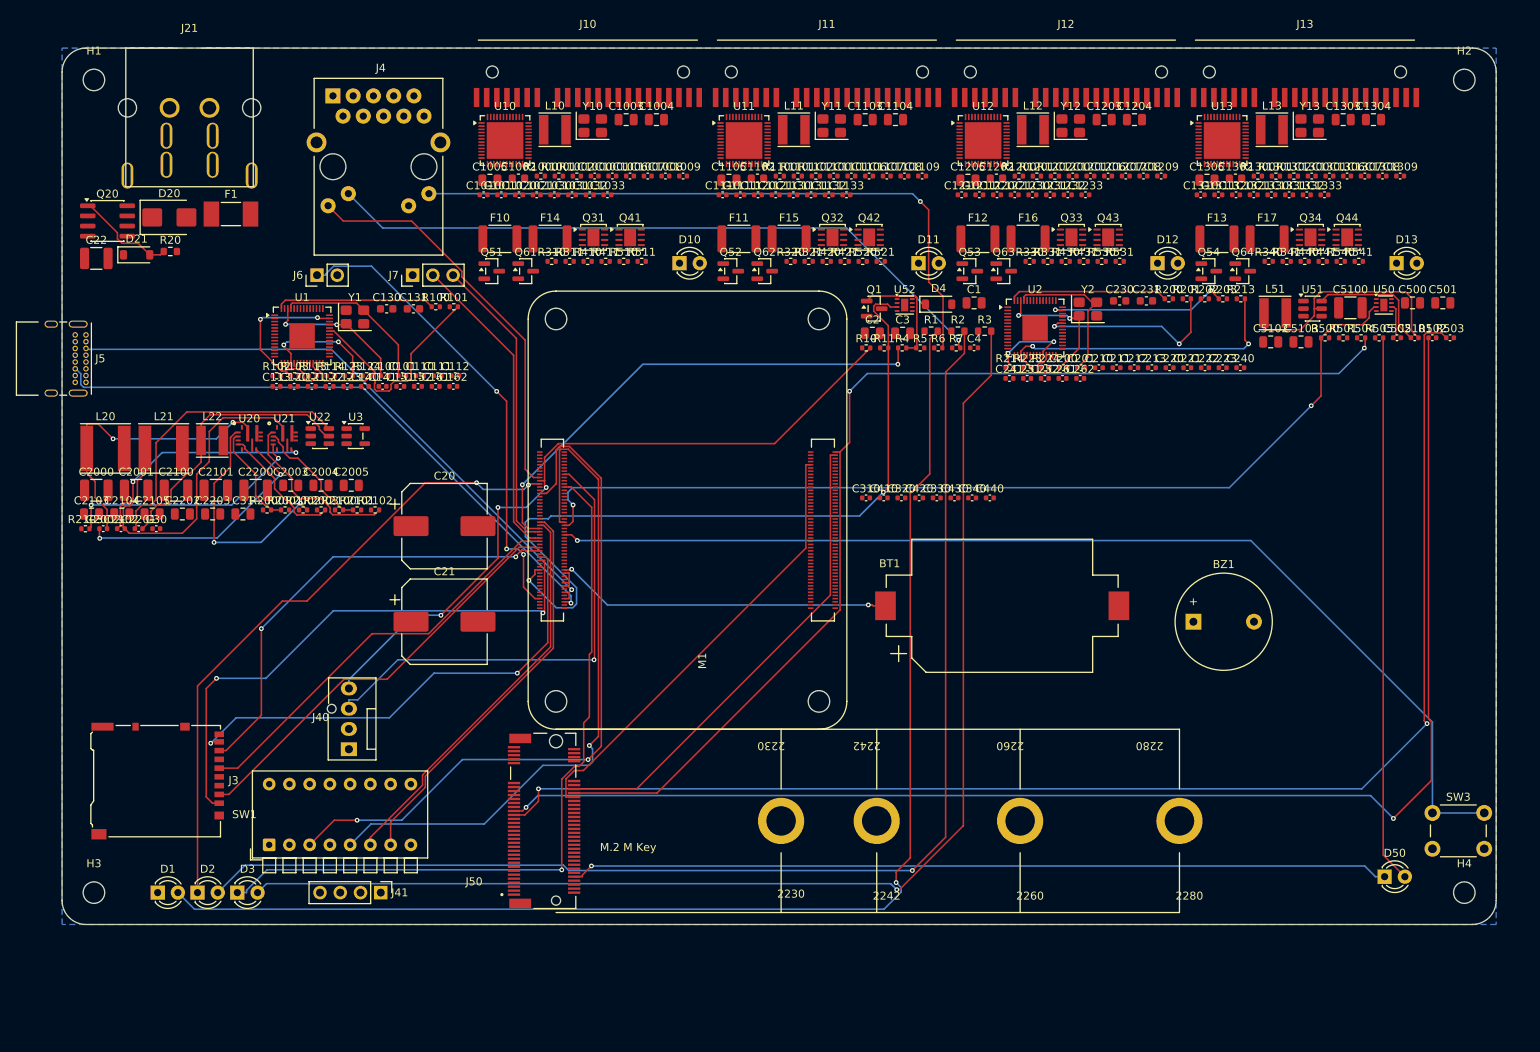
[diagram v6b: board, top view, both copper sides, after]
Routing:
- net M2_PERp0: track 0.00 -> 174.8 mm, vias 0 -> 2
- net M2_PERn0: track 0.00 -> 172.3 mm, vias 0 -> 2
- net D1_A: track 0.00 -> 165.4 mm, vias 0 -> 1
- net D2_A: track 0.00 -> 159.3 mm, vias 0 -> 1
- net D3_A: track 0.00 -> 156.2 mm, vias 0 -> 1
- net PCIE_CLKREQ: track 0.00 -> 139.6 mm, vias 0 -> 2
- net M2_DOOR: track 0.00 -> 136.6 mm, vias 0 -> 1
- net M2_PWR_EN: track 0.00 -> 121.0 mm, vias 0 -> 2
- net M2_DAS: track 0.00 -> 103.0 mm, vias 0 -> 1
- net SD_PWR_ON: track 0.00 -> 96.8 mm, vias 0 -> 2
- net STATUS_LED: track 0.00 -> 94.0 mm, vias 0 -> 1
- net FAN_PWM: track 0.00 -> 90.6 mm, vias 0 -> 3
- net DIP3: track 0.00 -> 89.7 mm, vias 0 -> 2
- net DIP5: track 0.00 -> 87.0 mm, vias 0 -> 1
- net ETH_LED_Y_A: track 0.00 -> 85.3 mm, vias 0 -> 1
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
